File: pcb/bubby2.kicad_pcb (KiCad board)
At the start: 2 copper layers, 7 parts, among them SW1 1825027-8, SW2 1825027-8, SW3 1825027-8, SW4 1825027-8, SW5 1825027-8, SW6 SW_SPST

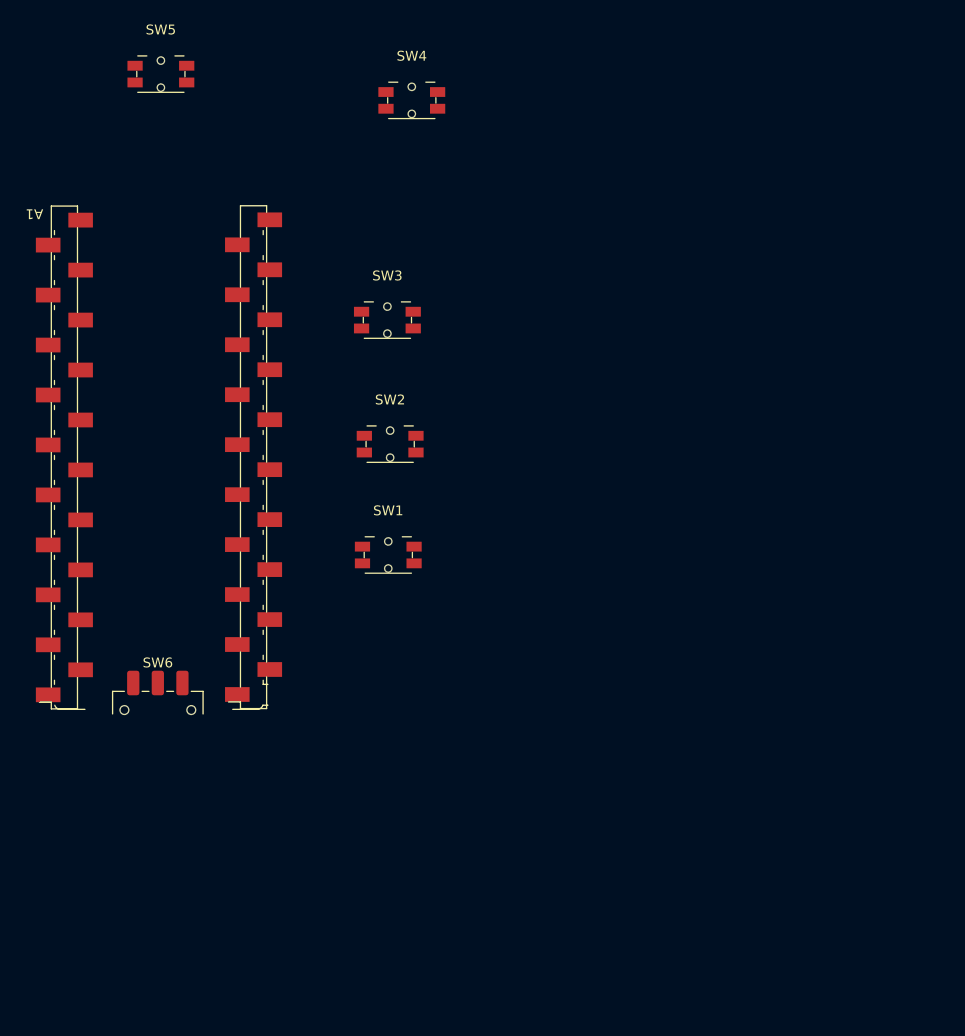
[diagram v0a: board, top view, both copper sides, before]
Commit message: pcb routed
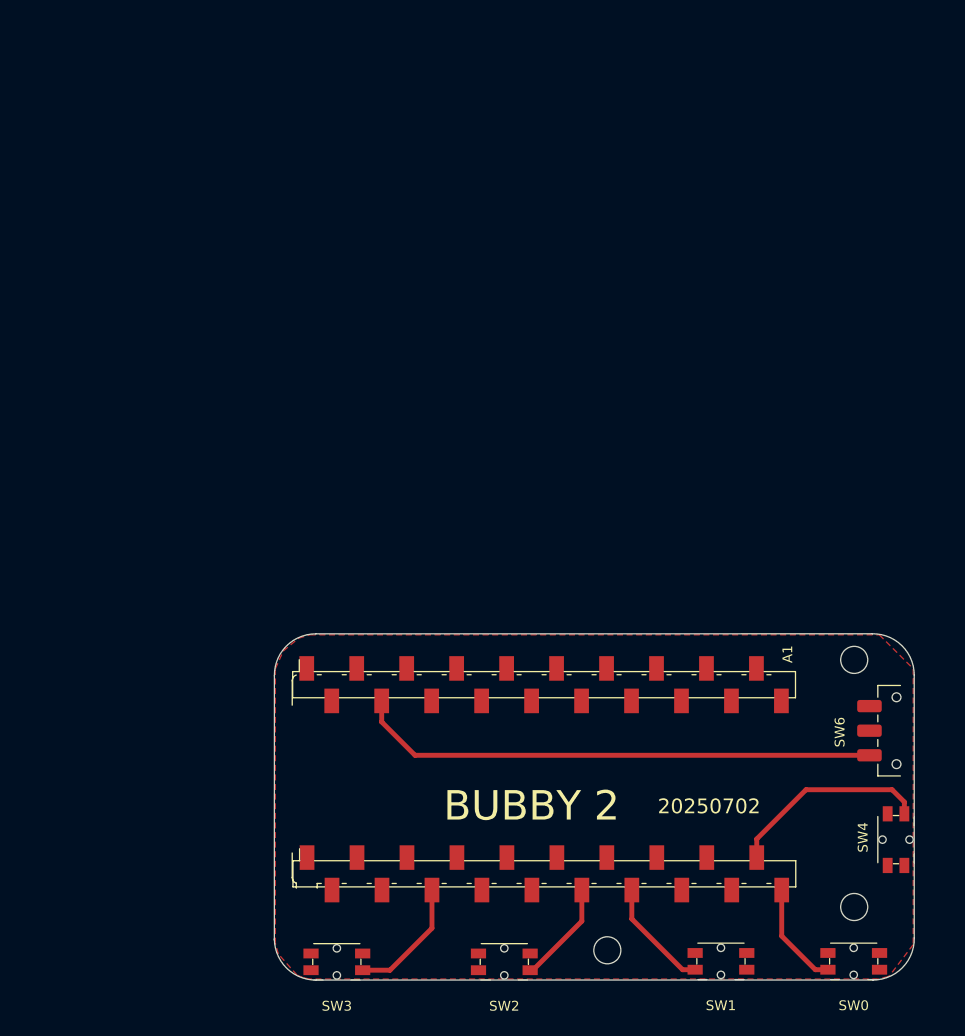
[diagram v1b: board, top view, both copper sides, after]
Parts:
- A1: value RaspberryPi_Pico -> RP2350-LCD-0.96
- moved SW4 107.9 mm to (249.3, 114.7), turned to -90 degrees
- moved SW0 98.4 mm to (245.0, 127.0), turned to 180 degrees
- moved SW6 75.1 mm to (249.3, 103.6), turned to 90 degrees
- moved SW1 73.5 mm to (231.5, 127.0), turned to 180 degrees
- moved SW2 53.9 mm to (209.5, 127.1), turned to 180 degrees
- moved A1 51.0 mm to (213.5, 108.5), turned to 90 degrees
- moved SW3 41.7 mm to (192.4, 127.1), turned to 180 degrees
- renumbered SW4 to SW0, SW3 to SW1, SW1 to SW3, SW5 to SW4
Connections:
- A1 pad 12: unconnected-(A1-GPIO9-Pad12) -> Net-(A1-GPIO9)
- A1 pad 14: unconnected-(A1-GPIO10-Pad14) -> Net-(A1-GPIO10)
- A1 pad 15: Net-(A1-GPIO11) -> unconnected-(A1-GPIO11-Pad15)
- A1 pad 16: Net-(A1-GPIO12) -> unconnected-(A1-GPIO12-Pad16)
- A1 pad 17: Net-(A1-GPIO13) -> unconnected-(A1-GPIO13-Pad17)
- A1 pad 6: unconnected-(A1-GPIO4-Pad6) -> Net-(A1-GPIO4)
- SW0 pad 1: Net-(A1-GPIO14) -> Net-(A1-GPIO15)
- SW1 pad 1: Net-(A1-GPIO13) -> Net-(A1-GPIO10)
- SW2 pad 1: Net-(A1-GPIO12) -> Net-(A1-GPIO9)
- SW3 pad 1: Net-(A1-GPIO11) -> Net-(A1-GPIO4)
- SW4 pad 1: Net-(A1-GPIO15) -> Net-(A1-GPIO14)
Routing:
- net Net-(A1-3V3_EN): track 0.00 -> 53.1 mm
- net Net-(A1-GPIO14): track 0.00 -> 20.7 mm
- net Net-(A1-GPIO4): track 0.00 -> 12.7 mm
- net Net-(A1-GPIO10): track 0.00 -> 11.5 mm
- net Net-(A1-GPIO15): track 0.00 -> 10.8 mm
- net Net-(A1-GPIO9): track 0.00 -> 10.5 mm
- added copper zone on F.Cu, net GND
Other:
- board outline added: 65.1 x 35.2 mm
- board text added: "20250702"
- board text added: "BUBBY 2"

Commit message: pretty close
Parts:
- moved SW0 0.89 mm to (244.8, 126.2)
- moved SW1 0.89 mm to (231.3, 126.2)
- moved SW2 0.89 mm to (209.3, 126.2)
- moved SW3 0.89 mm to (192.3, 126.2)
- moved SW4 0.62 mm to (248.7, 114.7)
- moved SW6 0.62 mm to (248.7, 103.6)
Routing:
- net Net-(A1-GPIO14): track 20.7 -> 19.8 mm
- net Net-(A1-GPIO15): track 10.8 -> 10.3 mm
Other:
- outline, holes or cut-outs redrawn

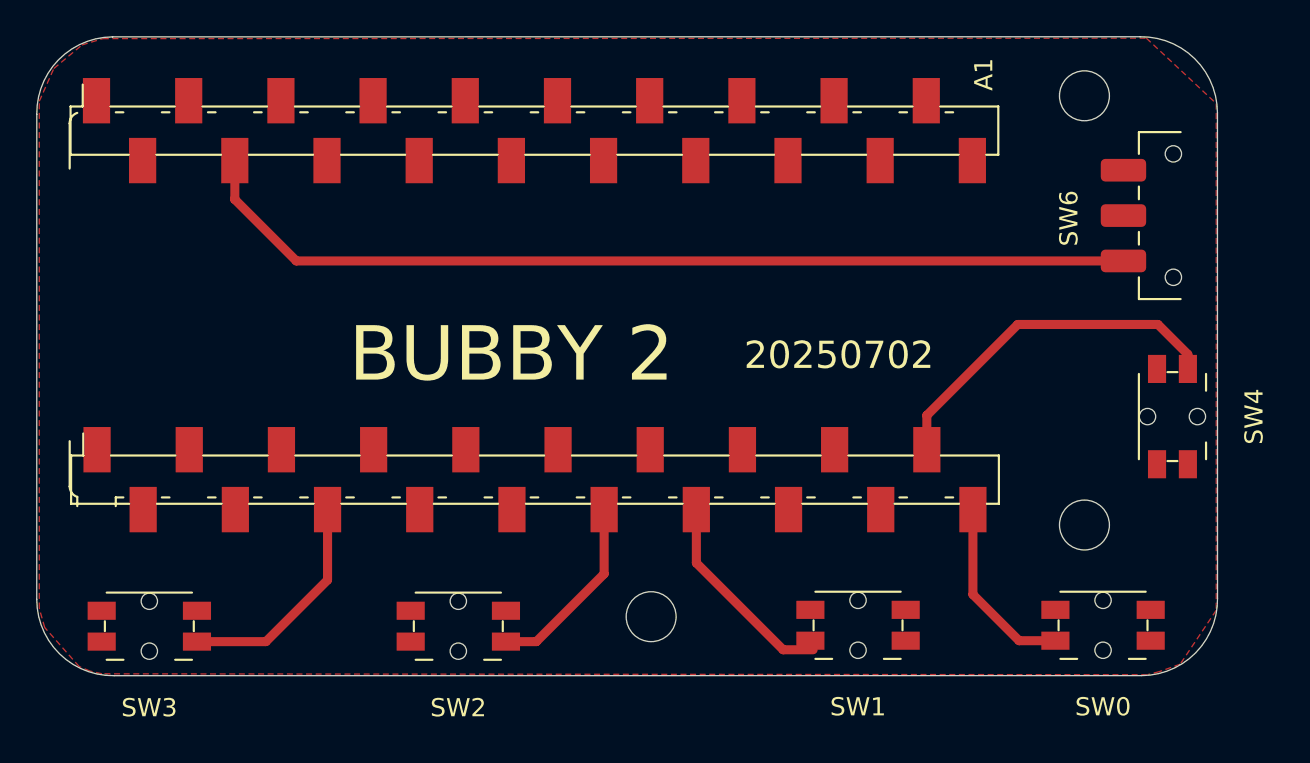
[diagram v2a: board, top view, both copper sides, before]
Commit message: no DRC errors!
changed schematic parts to remove all DRC issues.
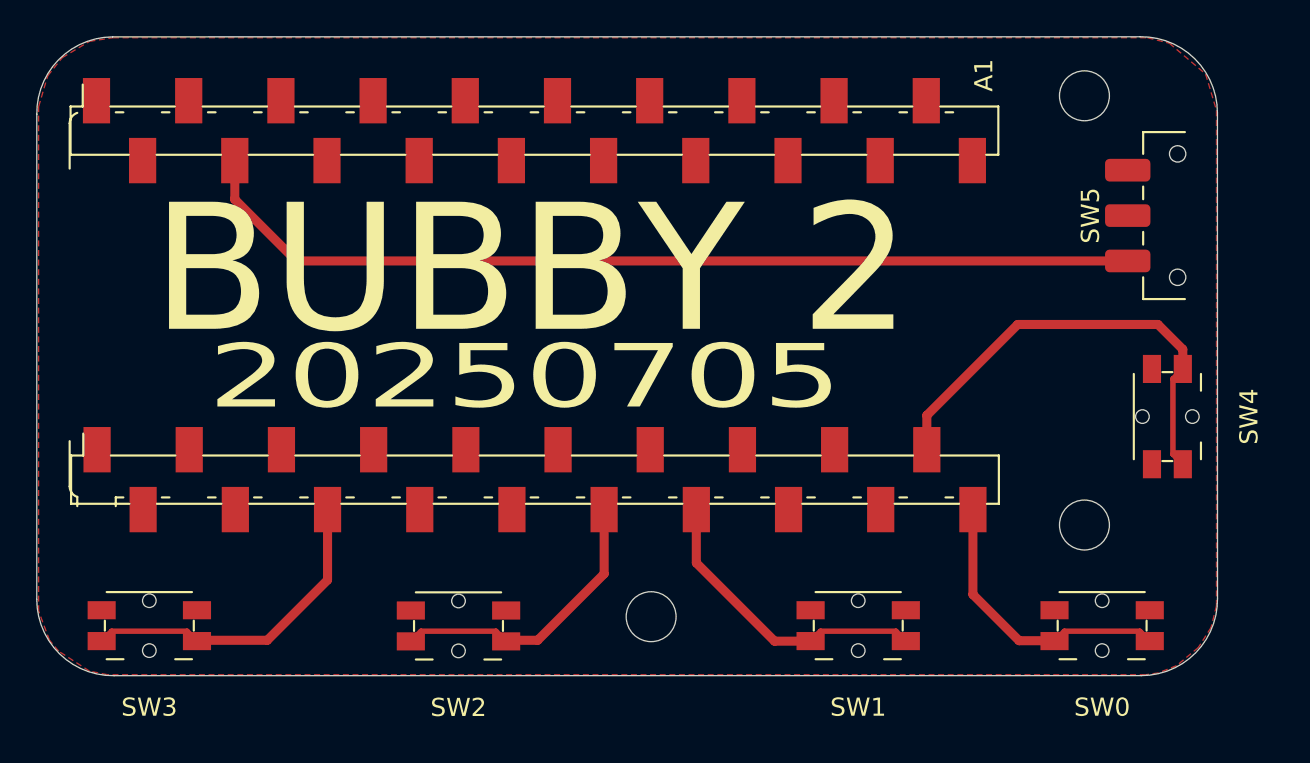
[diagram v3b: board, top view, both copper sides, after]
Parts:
- removed SW6: SW_SPST, footprints:sw_spdt_slide_mskt-12c03
- added SW5: SW_DPDT_x2, footprints:sw_spdt_slide_mskt-12c03, F.Cu at (249.0, 103.6)
- A1: value RP2350-LCD-0.96 -> RaspberryPi_Pico
- SW0, SW1, SW2, SW3, SW4: value 1825027-8 -> SW_SPST
- moved SW4 0.28 mm to (248.4, 114.7)
- moved SW0 0.05 mm to (244.8, 126.2)
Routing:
- net Net-(A1-GPIO9): track 10.5 -> 16.2 mm
- net Net-(A1-GPIO4): track 12.5 -> 18.2 mm
- net Net-(A1-GPIO15): track 10.3 -> 16.0 mm
- net Net-(A1-GPIO10): track 11.4 -> 16.7 mm
- net Net-(A1-GPIO14): track 19.8 -> 25.1 mm
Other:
- board text added: "20250705"
- board text removed: "20250702"

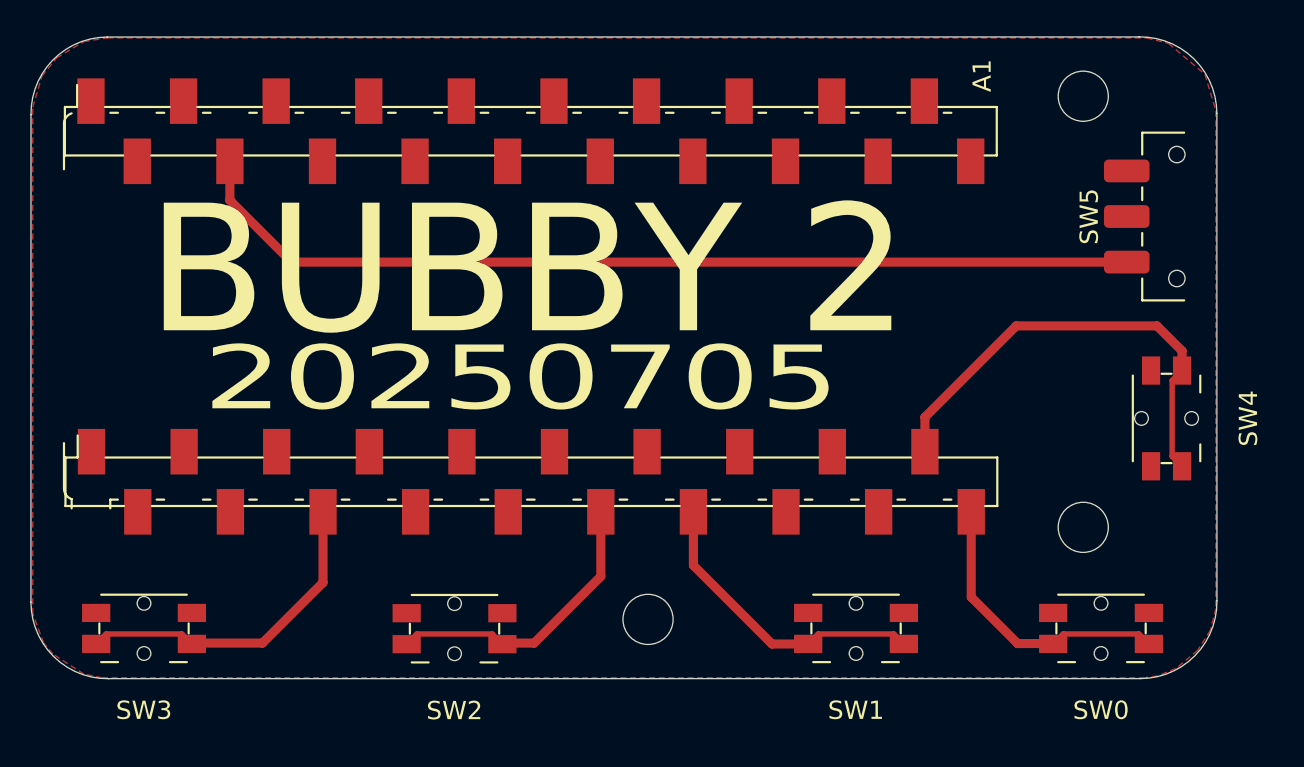
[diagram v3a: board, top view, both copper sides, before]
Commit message: case / mount hole move
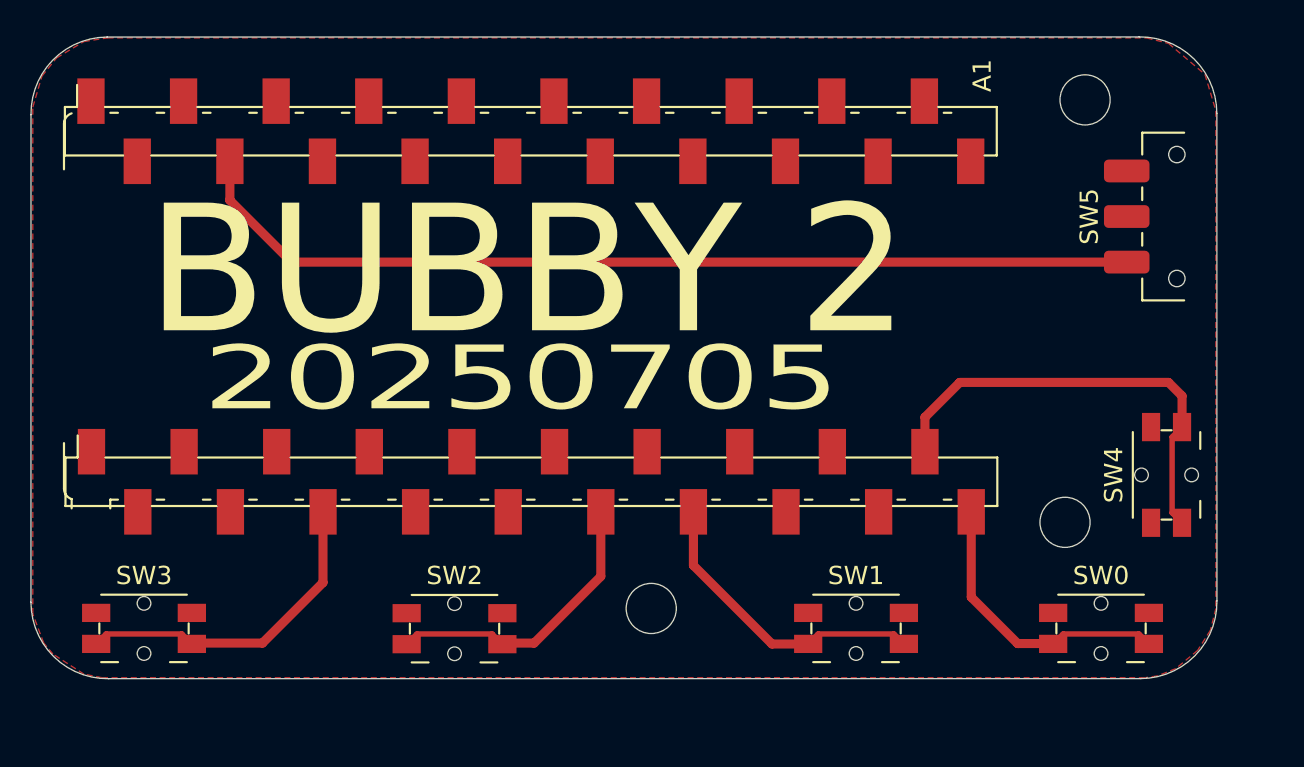
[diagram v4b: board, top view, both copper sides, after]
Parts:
- moved SW4 3.10 mm to (248.4, 117.8)
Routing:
- net Net-(A1-GPIO14): track 25.1 -> 24.5 mm
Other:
- outline, holes or cut-outs redrawn

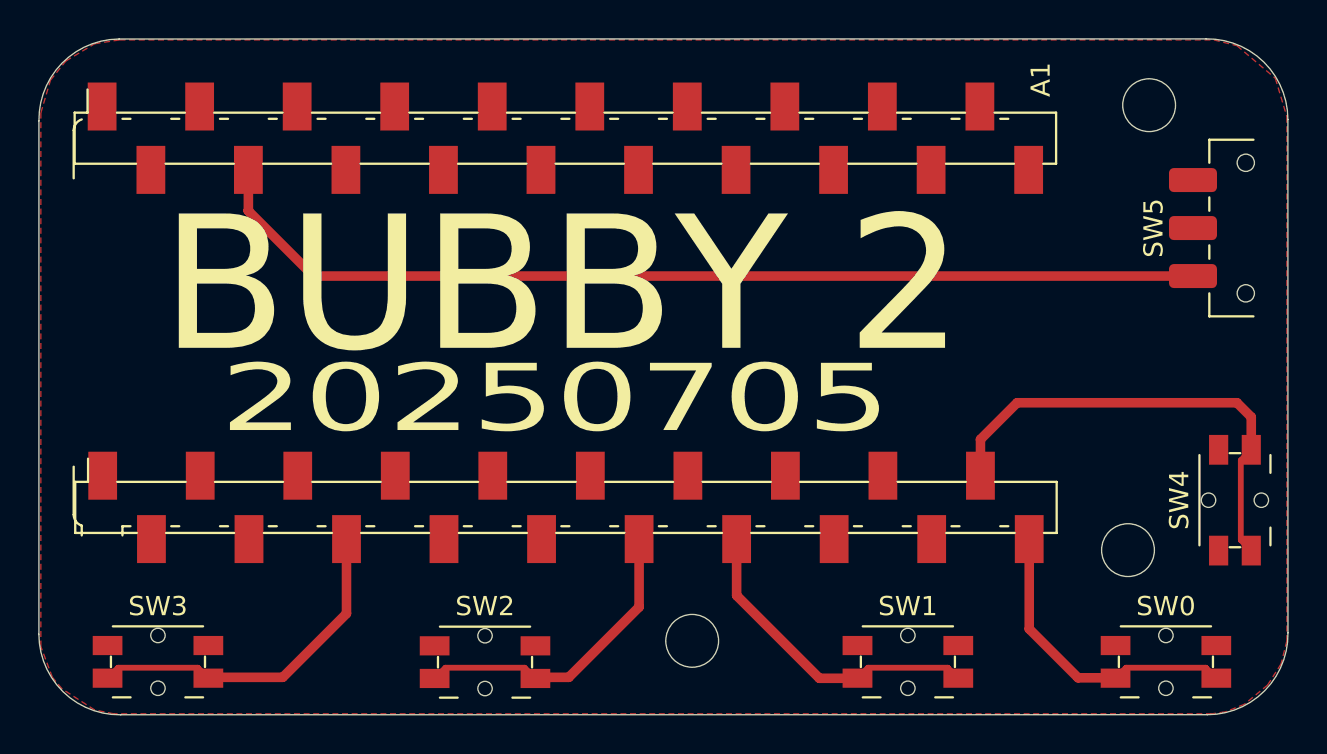
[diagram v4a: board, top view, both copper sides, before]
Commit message: pcb / cad
adjusting case buttons
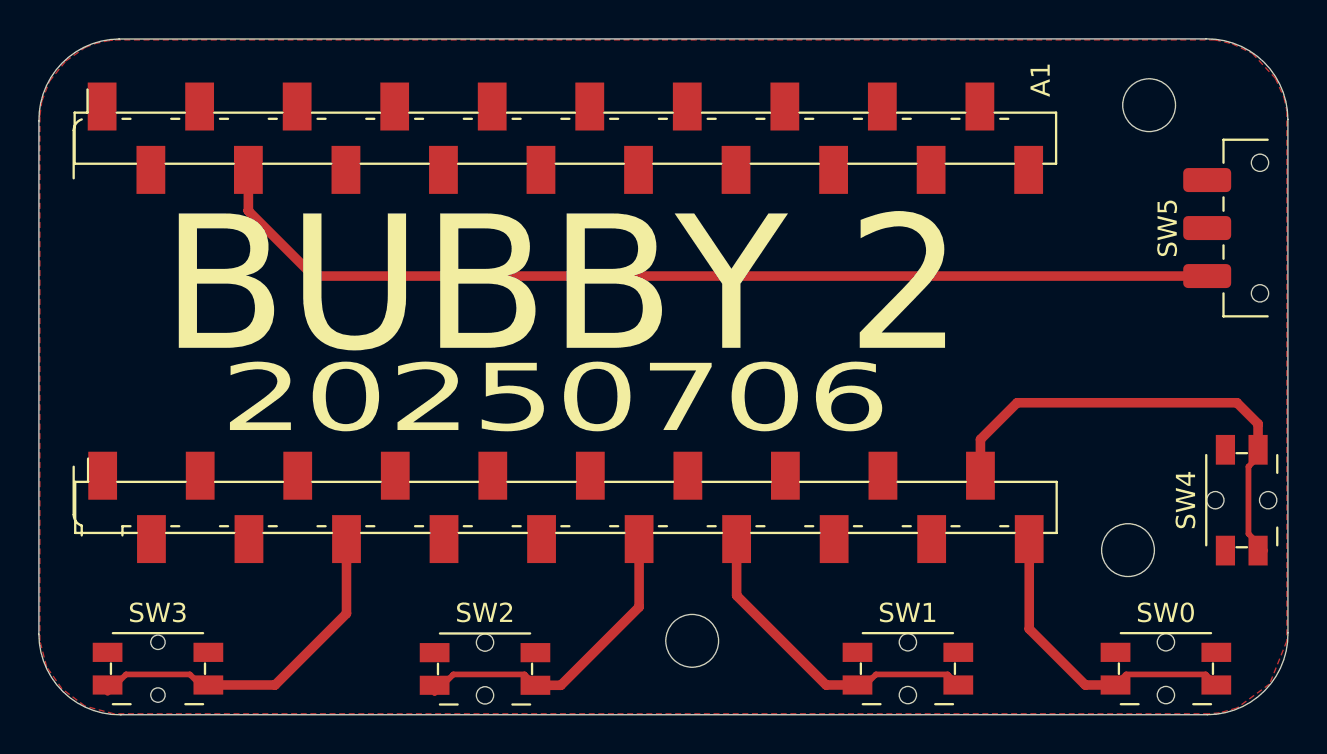
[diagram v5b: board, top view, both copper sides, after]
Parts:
- moved SW5 0.74 mm to (249.7, 103.6)
- moved SW0 0.36 mm to (244.8, 126.5)
- moved SW1 0.36 mm to (231.4, 126.5)
- moved SW2 0.36 mm to (209.3, 126.6)
- moved SW3 0.36 mm to (192.3, 126.5)
- moved SW4 0.35 mm to (248.8, 117.8)
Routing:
- net Net-(A1-GPIO14): track 24.5 -> 23.7 mm
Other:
- board text added: "20250706"
- board text removed: "20250705"
